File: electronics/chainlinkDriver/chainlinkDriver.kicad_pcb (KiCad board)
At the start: 2 copper layers, 198.1 x 30.5 mm, 65 parts, among them J10 Sensor C, J11 Sensor D, J12 Motor E, J13 Motor F, J14 Sensor E, J15 Sensor F, J16 Power, J17 Power, J18 Power, J19 Input, J20 Output, J3 Motor A, J5 Motor B, J6 Motor C, J7 Motor D, J8 Sensor A, J9 Sensor B, U1 74HC595, U10 TPL7407L, U2 TPL7407L, U3 74HC125, U4 74HC165, U5 74HC595, U6 TPL7407L, U7 74HC595, U8 TPL7407L, U9 74HC595

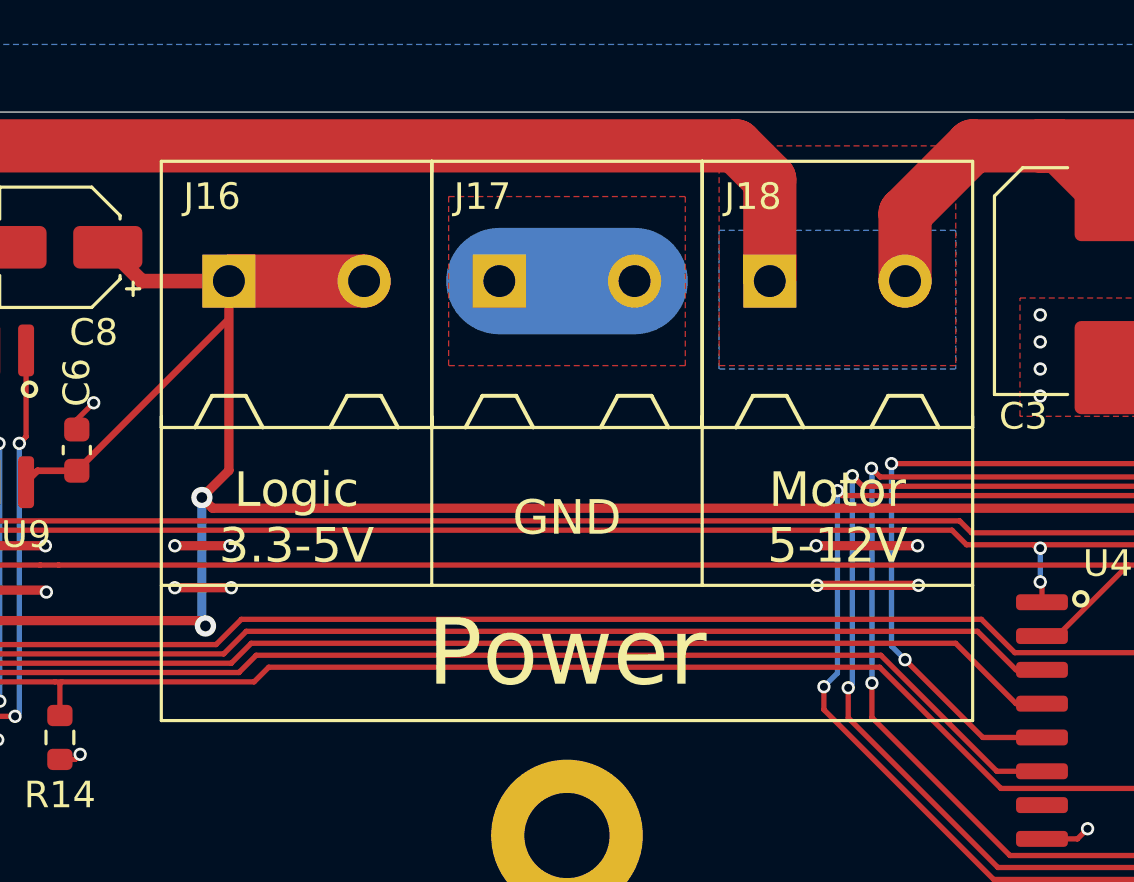
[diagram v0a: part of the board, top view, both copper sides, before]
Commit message: Add JLC alternatives for TPL7407L (ULN2003A) and screw terminal
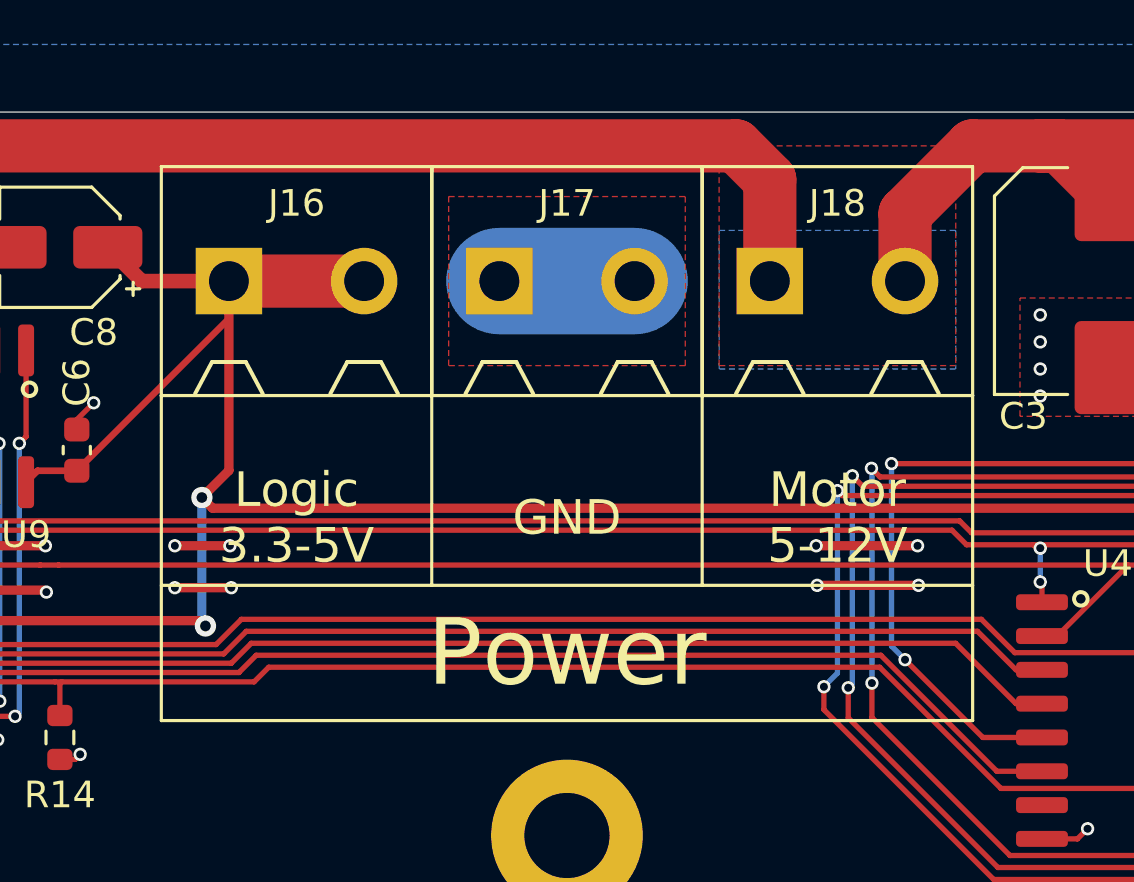
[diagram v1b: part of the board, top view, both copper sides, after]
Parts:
- J16, J17, J18: footprint ScrewTerminals:C8465_WJ500V-5.08-2P -> ScrewTerminals:Generic-5.08-2P
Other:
- board text added: "v1.1"
- board text removed: "[alpha]"

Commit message: Update values so LEDs, connectors can be grouped in BOM; add some LCSC alternative part numbers
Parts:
- D1: value LED A -> LED
- D2: value LED B -> LED
- D3: value LED C -> LED
- D4: value LED D -> LED
- D5: value LED E -> LED
- D6: value LED F -> LED
- J10: value Sensor C -> Sensor
- J11: value Sensor D -> Sensor
- J12: value Motor E -> Motor
- J13: value Motor F -> Motor
- J14: value Sensor E -> Sensor
- J15: value Sensor F -> Sensor
- J19: value Input -> IDC
- J20: value Output -> IDC
- J3: value Motor A -> Motor
- J5: value Motor B -> Motor
- J6: value Motor C -> Motor
- J7: value Motor D -> Motor
- J8: value Sensor A -> Sensor
- J9: value Sensor B -> Sensor

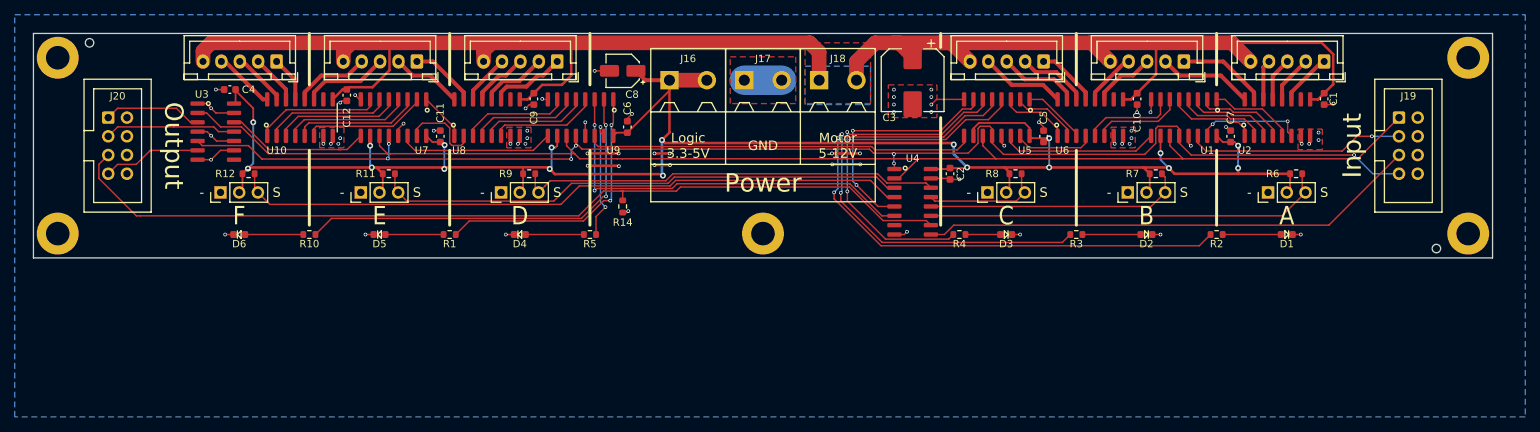
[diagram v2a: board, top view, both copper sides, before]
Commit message: Output enable ChainlinkDriver
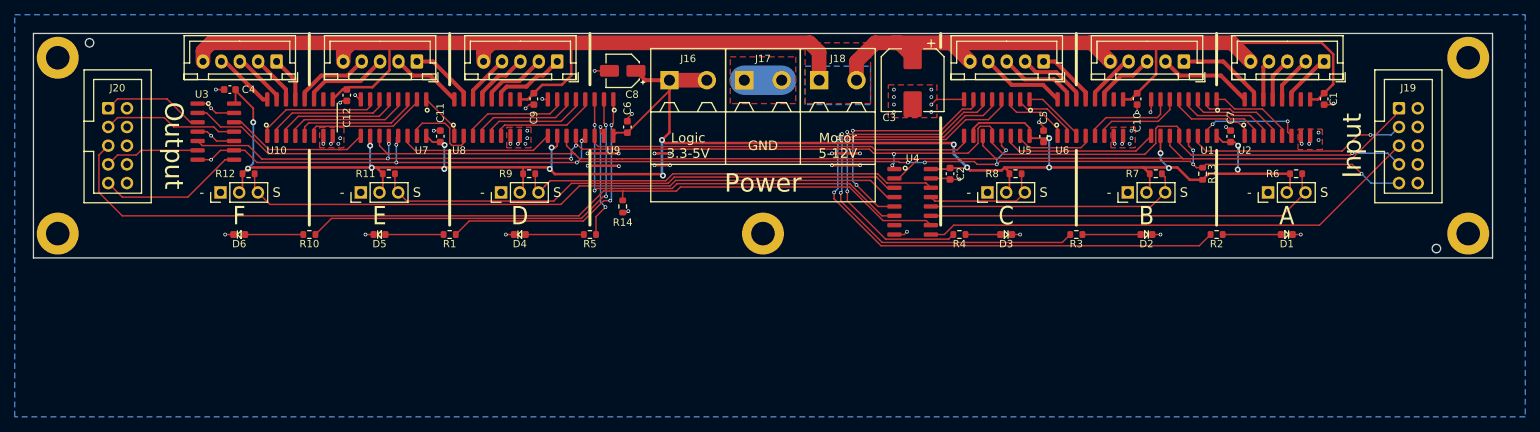
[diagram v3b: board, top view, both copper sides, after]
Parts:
- added R13: 47k, Resistor_SMD:R_0603_1608Metric, F.Cu at (184.2, 44.5)
- J19, J20: footprint ModifiedSymbols:IDC-Header_2x04_P2.54mm_Vertical -> ModifiedSymbols:IDC-Header_2x05_P2.54mm_Vertical_2x04Silk
- moved J19 1.27 mm to (210.8, 35.6)
- moved J20 1.27 mm to (35.6, 35.6)
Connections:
- U1 pad 13: GND -> /nOE_IN
- U3 pad 8: (no net) -> /nOE_OUT
- U3 pad 9: GND -> /nOE_IN
- U5 pad 13: GND -> /nOE_IN
- U7 pad 13: GND -> /nOE_IN
- U9 pad 13: GND -> /nOE_IN
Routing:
- net /nOE_IN: track 0.00 -> 177.2 mm, vias 0 -> 11
- net /nOE_OUT: track 0.00 -> 20.0 mm
- net GND: track 82.8 -> 76.1 mm, vias 67 -> 63
- net /SENSOR_IN: track 123.8 -> 126.2 mm
- net +3V3: track 267.1 -> 268.2 mm
- net /CLOCK_IN: track 188.1 -> 188.9 mm
- net /SENSOR_OUT: track 68.0 -> 68.6 mm
- net /CLOCK_OUT: track 13.4 -> 14.0 mm
- net /LATCH_OUT: track 13.4 -> 12.9 mm
- net /MOTOR_IN: track 29.6 -> 30.1 mm
- net /MOTOR_OUT: track 17.9 -> 18.4 mm
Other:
- board text added: "v1.2"
- board text removed: "v1.1"
